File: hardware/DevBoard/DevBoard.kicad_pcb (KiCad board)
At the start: 2 copper layers, 93.5 x 90.5 mm, 8 parts, among them J1 Conn_02x06_Odd_Even, J2 Conn_02x06_Odd_Even, J3 Conn_02x01, J4 Conn_01x10, J5 Conn_01x07, U1 Adafruit_SD_Breakout, U2 nRF52840-Feather-Sense, U3 ADS1299EEGFE-PDK

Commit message: Added revision and 'Not for use as a medical device' to the silkscreen.
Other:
- board text added: "VolksEEG DevBoard - Rev 01 Not for use as a medical device."
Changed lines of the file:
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@@
   )
   (gr_rect (start 136.906 61.468) (end 230.396 152) (layer "Edge.Cuts") (width 0.1) (fill none))
+  (gr_text "VolksEEG DevBoard - Rev 01\nNot for use as a medical device." (at 162.052 92.456) (layer "F.SilkS")
+    (effects (font (size 1.5 1.5) (thickness 0.3)))
+  )
   (segment (start 145 118.364) (end 146.27 117.094) (width 0.5) (layer "F.Cu") (net 1))
   (segment (start 146.27 117.094) (end 145 115.824) (width 0.5) (layer "F.Cu") (net 1))

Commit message: adjusted board dimensions slightly and regenerated Gerbers.
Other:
- board size 93.5 x 90.5 mm -> 91 x 88 mm
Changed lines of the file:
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@@
     )
   )
-  (gr_rect (start 136.906 61.468) (end 230.396 152) (layer "Edge.Cuts") (width 0.1) (fill none))
+  (gr_rect (start 137.5 61) (end 228.5 149) (layer "Edge.Cuts") (width 0.1) (fill none))
   (gr_text "VolksEEG DevBoard - Rev 01\nNot for use as a medical device." (at 162.052 92.456) (layer "F.SilkS")
     (effects (font (size 1.5 1.5) (thickness 0.3)))
@@
     (polygon
       (pts
-        (xy 230.378 151.892)
-        (xy 136.906 151.892)
-        (xy 136.906 61.468)
-        (xy 230.378 61.468)
+        (xy 228.6 148.844)
+        (xy 137.668 148.844)
+        (xy 137.668 60.96)
+        (xy 228.6 60.96)
       )
     )

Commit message: Updates
WIP
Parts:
- added J6: Conn_02x06_Odd_Even, VolksEEG:6-Jumper Header, F.Cu at (125.7, 43.2)
- added Mnt1: MountingHole_2.2mm_M2, MountingHole:MountingHole_2.2mm_M2, F.Cu at (103.0, 29.0)
- added Mnt2: MountingHole_2.2mm_M2, MountingHole:MountingHole_2.2mm_M2, F.Cu at (227.0, 29.0)
- added Mnt3: MountingHole_2.2mm_M2, MountingHole:MountingHole_2.2mm_M2, F.Cu at (227.0, 146.0)
- added Mnt4: MountingHole_2.2mm_M2, MountingHole:MountingHole_2.2mm_M2, F.Cu at (103.0, 146.0)
- added SW1: Tact-Switch, VolksEEG:Sparkfun Tactile Switch, F.Cu at (198.1, 33.0)
- added SW2: Tact-Switch, VolksEEG:Sparkfun Tactile Switch, F.Cu at (198.1, 50.8)
- added SW3: Tact-Switch, VolksEEG:Sparkfun Tactile Switch, F.Cu at (218.4, 43.2)
- added SW4: Tact-Switch, VolksEEG:Sparkfun Tactile Switch, F.Cu at (169.0, 66.0)
- added SW5: Tact-Switch, VolksEEG:Sparkfun Tactile Switch, F.Cu at (149.0, 66.0)
- added SW6: Reset Switch, VolksEEG:Sparkfun Tactile Switch, F.Cu at (112.0, 40.0)
- added U4: Adafruit-4650-FeatherWing-128x64, VolksEEG:nRF52840_Feather_Sense, F.Cu at (163.8, 43.2)
- moved J5 50.7 mm to (127.0, 96.5), turned to 90 degrees
- moved J1 39.2 mm to (120.7, 87.6), turned to -90 degrees
- moved U1 37.2 mm to (116.8, 71.1)
- moved J3 12.4 mm to (193.0, 61.0)
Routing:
- net /5V_ads: track 154.8 -> 0.00 mm
- net /~{DRDY_ads}: track 114.1 -> 0.00 mm, vias 1 -> 0
- net /~{CS_ads}: track 98.3 -> 0.00 mm, vias 1 -> 0
- net /MOSI: track 67.6 -> 0.00 mm, vias 1 -> 0
- net /MISO: track 66.5 -> 0.00 mm, vias 1 -> 0
- net /~{CS_sdc}: track 64.8 -> 0.00 mm
- net /SCK: track 57.4 -> 0.00 mm, vias 1 -> 0
- net /5V_sdc: track 54.3 -> 0.00 mm
- net /~{CD_sdc}: track 53.7 -> 0.00 mm
- net /3V3_ads: track 51.3 -> 0.00 mm
- net /3V3_sdc: track 43.2 -> 0.00 mm
- net /GND: track 40.5 -> 0.00 mm, vias 1 -> 0
- net /SDA_nrf: track 31.3 -> 0.00 mm
- net /SCL_nrf: track 31.3 -> 0.00 mm
- net /3V3_nrf: track 31.0 -> 0.00 mm
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- removed copper zone on B.Cu, net /GND
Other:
- board size 91 x 88 mm -> 134 x 127 mm
- board text added: "Battery"
- board text added: "Down"
- board text added: "Reset"
- board text added: "Select"
- board text added: "Up"

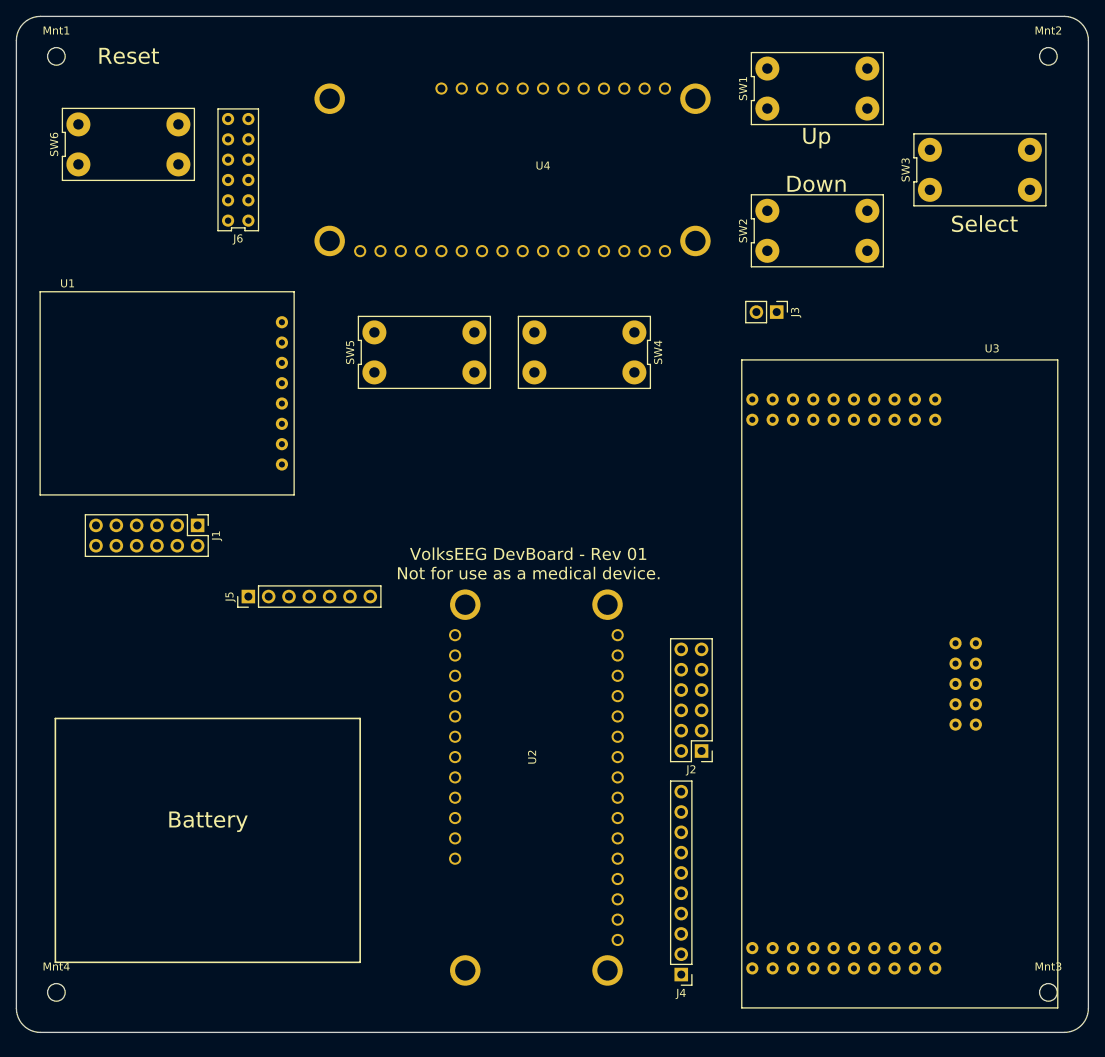
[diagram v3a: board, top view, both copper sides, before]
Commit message: Ready for schematic review
Besides changing net names and so forth:
- Changed Feather 3V pin to output
- Added ADS1299EEGFE-PDK to VolksEEG symbol library
- Added Adafruit_SD_Breakout to VolksEEG symbol library

ERC complains that three switches should be updated from library, can't seem to fix that
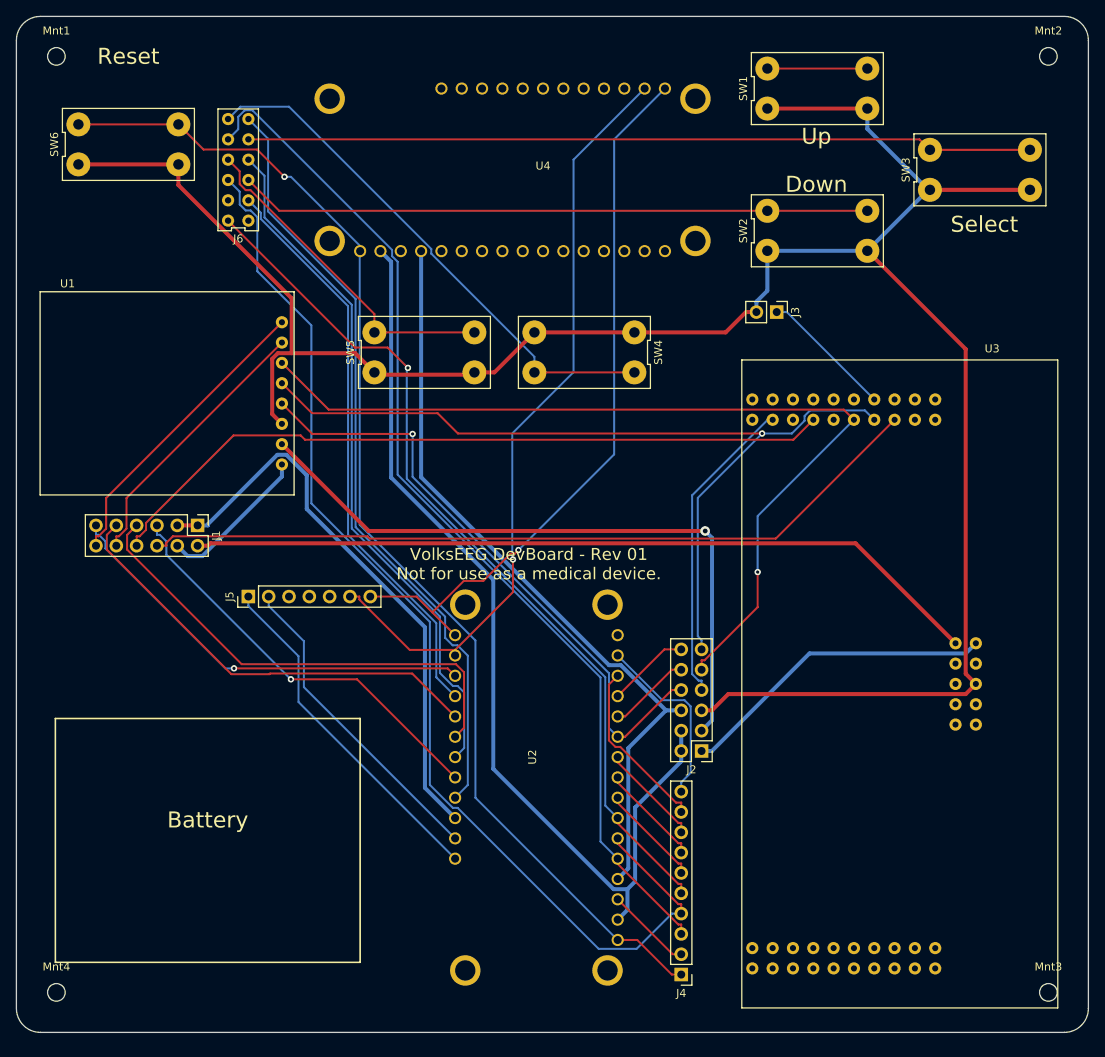
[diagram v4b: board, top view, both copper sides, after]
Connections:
- J6 pad 2: /GPIO6_nrf -> /SW1_nrf
- J6 pad 4: /GPIO11_nrf -> /SW2_nrf
- J6 pad 6: /GPIO13_nrf -> /SW3_nrf
- SW1 pad 3: /sw1 -> /sw_a
- SW1 pad 4: /sw1 -> /sw_a
- U1 pad 4: /SCK -> /SCK_nrf
- U2 pad 20: /GPIO6_nrf -> /SW1_nrf
- U2 pad 23: /GPIO11_nrf -> /SW2_nrf
- U2 pad 25: /GPIO13_nrf -> /SW3_nrf
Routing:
- net /GND: track 0.00 -> 281.2 mm
- net /RST_nrf: track 0.00 -> 151.4 mm, vias 0 -> 1
- net /A1_nrf: track 0.00 -> 141.1 mm
- net /A0_nrf: track 0.00 -> 130.8 mm
- net /3V3_nrf: track 0.00 -> 120.5 mm
- net /MOSI: track 0.00 -> 113.8 mm, vias 0 -> 1
- net /A2_nrf: track 0.00 -> 110.3 mm, vias 0 -> 1
- net /MISO: track 0.00 -> 109.2 mm, vias 0 -> 1
- net /5V_ads: track 0.00 -> 100.0 mm
- net /~{DRDY_ads}: track 0.00 -> 99.2 mm
- net /sw3: track 0.00 -> 98.2 mm
- net /SW3_nrf: track 0.00 -> 97.2 mm
- net /SCL_nrf: track 0.00 -> 96.9 mm, vias 0 -> 1
- net /GND_nrf: track 0.00 -> 96.4 mm
- net /~{CS_ads}: track 0.00 -> 92.7 mm
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
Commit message: As sent to JLBPC
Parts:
- moved U2 8.50 mm to (154.7, 118.4)
- moved J5 5.57 mm to (121.9, 94.2)
- moved J2 4.10 mm to (179.6, 115.3)
- moved Mnt1 2.83 mm to (105.0, 31.0)
- moved Mnt2 2.83 mm to (225.0, 31.0)
- moved Mnt3 2.83 mm to (225.0, 144.0)
- moved Mnt4 2.83 mm to (105.0, 144.0)
- moved J4 1.78 mm to (179.3, 143.8)
- moved J1 1.01 mm to (120.7, 86.6)
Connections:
- J6 pad 12: /A2_nrf -> /RST_nrf
- J6 pad 2: /SW1_nrf -> /GPIO6_nrf
- J6 pad 4: /SW2_nrf -> /GPIO11_nrf
- J6 pad 6: /SW3_nrf -> /GPIO13_nrf
- SW1 pad 3: /sw_a -> /sw1
- SW1 pad 4: /sw_a -> /sw1
- SW6 pad 3: /RST_nrf -> /sw6
- SW6 pad 4: /RST_nrf -> /sw6
- U2 pad 20: /SW1_nrf -> /GPIO6_nrf
- U2 pad 23: /SW2_nrf -> /GPIO11_nrf
- U2 pad 25: /SW3_nrf -> /GPIO13_nrf
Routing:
- net /GPIO13_nrf: track 0.00 -> 98.4 mm, vias 0 -> 1
- net /SW3_nrf: track 97.2 -> 0.00 mm
- net /sw1: track 0.00 -> 93.0 mm
- net /A2_nrf: track 110.3 -> 17.6 mm, vias 1 -> 0
- net /GPIO11_nrf: track 0.00 -> 87.6 mm
- net /SW2_nrf: track 86.7 -> 0.00 mm
- net /SW1_nrf: track 72.7 -> 0.00 mm
- net /GPIO6_nrf: track 0.00 -> 71.0 mm
- net /sw6: track 0.00 -> 24.8 mm
- net /RST_nrf: track 151.4 -> 132.2 mm, vias 1 -> 0
- net /sw_a: track 12.5 -> 0.00 mm
- net /TX_nrf: track 22.9 -> 34.7 mm
- net /~{ADS_CS_nrf}: track 60.5 -> 49.0 mm, vias 0 -> 1
- net /A1_nrf: track 141.1 -> 151.3 mm
- net /MISO: track 109.2 -> 119.4 mm, vias 1 -> 0
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- added copper zone on B.Cu, net /GND
- added copper zone on F.Cu, net /GND
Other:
- board text added: "3.3V"
- board text added: "3V3_ADS"
- board text added: "3V3_NRF"
- board text added: "3V3_SDC"
- board text added: "A0_NRF"
- board text added: "A1_NRF"
- board text added: "A2_NRF"
- board text added: "A3_NRF"
- board text added: "A4_NRF"
- board text added: "A5_NRF"
- board text added: "AREF_NRF"
- board text added: "BAT_NRF"
- board text added: "EN_NRF"
- board text added: "GND"
- board text added: "GND_NRF"
- board text added: "GPIO11_NRF"
- board text added: "GPIO13_NRF"
- board text added: "GPIO6_NRF"
- board text added: "MISO"
- board text added: "MISO_NRF"
- board text added: "MOSI"
- board text added: "MOSI_NRF"
- board text added: "RST"
- board text added: "RST_NRF"
- board text added: "RX_NRF"
- board text added: "SCK"
- board text added: "SCK_NRF"
- board text added: "SCL"
- board text added: "SCL_NRF"
- board text added: "SDA"
- board text added: "SDA_NRF"
- board text added: "TX_NRF"
- board text added: "VolksEEG DevBoard - Rev 02 Not for use as a medical device."
- board text removed: "VolksEEG DevBoard - Rev 01 Not for use as a medical device."
